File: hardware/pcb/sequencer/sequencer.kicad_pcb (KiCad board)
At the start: 2 copper layers, 106 parts, among them J1 Conn_02x08_Counter_Clockwise, J2 Conn_02x08_Counter_Clockwise, SW1 SW_SPST, SW10 SW_SPST, SW11 SW_SPST, SW12 SW_SPST, SW13 SW_SPST, SW14 SW_SPST, SW15 SW_SPST, SW16 SW_SPST, SW17 SW_SPST, SW18 SW_SPST, SW19 SW_SPST, SW2 SW_SPST, SW20 SW_SPST, SW21 SW_SPST, SW22 SW_SPST, SW23 SW_SPST, SW24 SW_SPST, SW3 SW_SPST, SW4 SW_SPST, SW5 SW_SPST, SW6 SW_SPST, SW7 SW_SPST, SW8 SW_SPST, SW9 SW_SPST

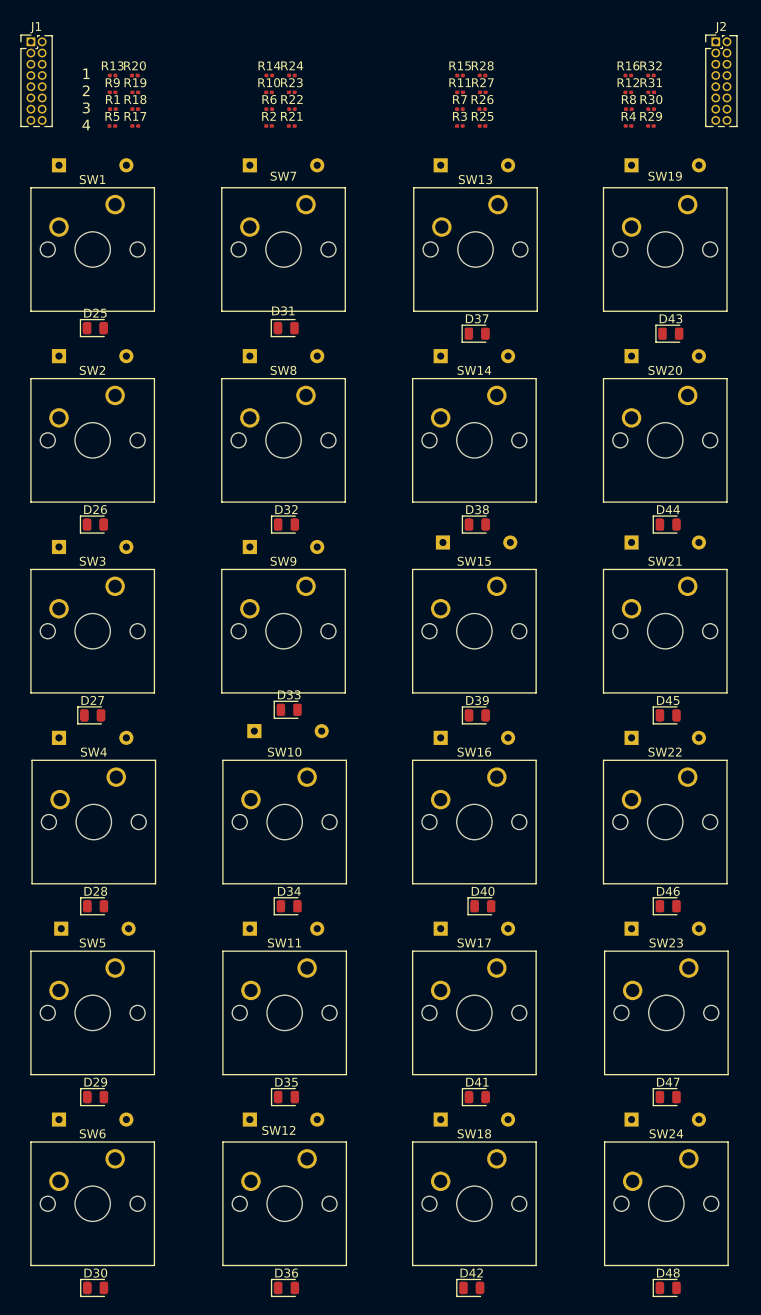
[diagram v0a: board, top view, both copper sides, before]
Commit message: sequencer: update pcb layout
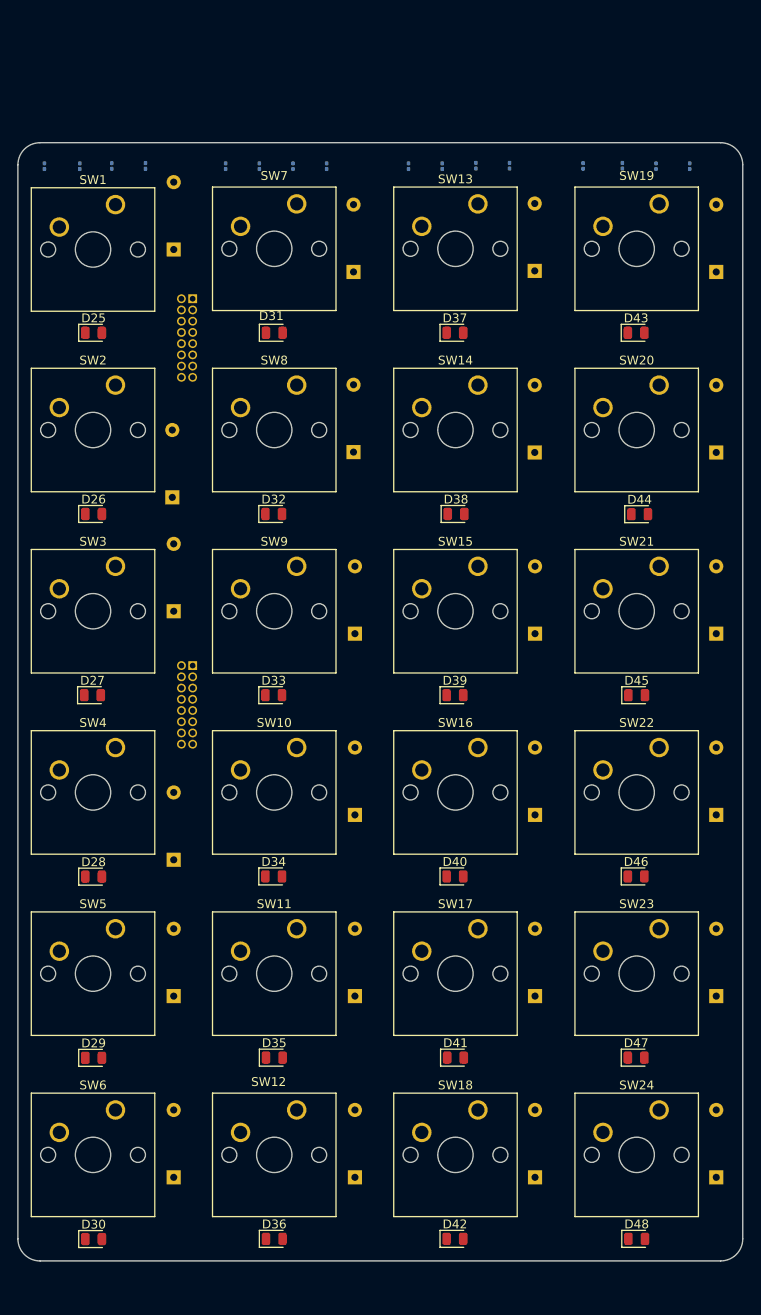
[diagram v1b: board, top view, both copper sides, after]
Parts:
- removed R17, R18, R19, R20, R21, R22, R23, R24, R25, R26, R27, R28, R29, R30, R31, R32: R, Resistor_SMD:R_0201_0603Metric
- J1, J2: value Conn_02x08_Counter_Clockwise -> Conn_02x08_Odd_Even; moved to B.Cu
- S1: renamed from R13; moved to B.Cu
- S10: renamed from R6; moved to B.Cu
- S11: renamed from R7; moved to B.Cu
- S12: renamed from R8; moved to B.Cu
- S13: renamed from R1; moved to B.Cu
- S14: renamed from R2; moved to B.Cu
- S15: renamed from R3; moved to B.Cu
- S16: renamed from R4; moved to B.Cu
- S2: renamed from R14; moved to B.Cu
- S3: renamed from R15; moved to B.Cu
- S4: renamed from R16; moved to B.Cu
- S5: renamed from R9; moved to B.Cu
- S6: renamed from R10; moved to B.Cu
- S7: renamed from R11; moved to B.Cu
- S8: renamed from R12; moved to B.Cu
- S9: renamed from R5; moved to B.Cu
- moved J2 92.1 mm to (72.3, 115.7), turned to 180 degrees
- moved J1 34.3 mm to (72.3, 74.2), turned to 180 degrees
- moved D2 20.5 mm to (70.0, 96.6), turned to 90 degrees
- moved D4 18.9 mm to (70.1, 137.6), turned to 90 degrees
- moved D7 16.8 mm to (90.5, 71.1), turned to 90 degrees
- moved D1 16.1 mm to (70.1, 68.6), turned to 90 degrees
- moved D13 16.0 mm to (111.0, 71.0), turned to 90 degrees
- moved D8 16.0 mm to (90.5, 91.5), turned to 90 degrees
- moved D9 15.4 mm to (90.6, 112.0), turned to 90 degrees
- moved D19 15.4 mm to (131.5, 71.1), turned to 90 degrees
- moved D14 15.2 mm to (111.0, 91.5), turned to 90 degrees
- moved D3 14.9 mm to (70.1, 109.5), turned to 90 degrees
- moved D5 14.8 mm to (70.1, 153.0), turned to 90 degrees
- moved D10 14.8 mm to (90.6, 132.5), turned to 90 degrees
- moved D15 14.7 mm to (111.0, 112.0), turned to 90 degrees
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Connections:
- D25 pad 2: Net-(D25-A) -> C1
- D26 pad 2: Net-(D25-A) -> C1
- D27 pad 2: Net-(D25-A) -> C1
- D28 pad 2: Net-(D25-A) -> C1
- D29 pad 2: Net-(D25-A) -> C1
- D30 pad 2: Net-(D25-A) -> C1
- D31 pad 2: Net-(D31-A) -> C2
- D32 pad 2: Net-(D31-A) -> C2
- D33 pad 2: Net-(D31-A) -> C2
- D34 pad 2: Net-(D31-A) -> C2
- D35 pad 2: Net-(D31-A) -> C2
- D36 pad 2: Net-(D31-A) -> C2
- D37 pad 2: Net-(D37-A) -> C3
- D38 pad 2: unconnected-(D38-A-Pad2) -> C3
- D39 pad 2: unconnected-(D39-A-Pad2) -> C3
- D40 pad 2: unconnected-(D40-A-Pad2) -> C3
- D41 pad 2: unconnected-(D41-A-Pad2) -> C3
- D42 pad 2: Net-(D37-A) -> C3
- D43 pad 2: Net-(D43-A) -> C4
- D44 pad 2: Net-(D43-A) -> C4
- D45 pad 2: Net-(D43-A) -> C4
- D46 pad 2: Net-(D43-A) -> C4
- D47 pad 2: Net-(D43-A) -> C4
- D48 pad 2: Net-(D43-A) -> C4
- J1 pad 10: I10 -> I13
- J1 pad 11: I11 -> I6
- J1 pad 12: I12 -> I14
- J1 pad 13: I13 -> I7
- J1 pad 14: I14 -> I15
- J1 pad 15: I15 -> I8
- J1 pad 2: I2 -> I9
- J1 pad 3: I3 -> I2
- J1 pad 4: I4 -> I10
- J1 pad 5: I5 -> I3
- J1 pad 6: I6 -> I11
- J1 pad 7: I7 -> I4
- J1 pad 8: I8 -> I12
- J1 pad 9: I9 -> I5
- J2 pad 10: O10 -> O13
- J2 pad 11: O11 -> O6
- J2 pad 12: O12 -> O14
- J2 pad 13: O13 -> O7
- J2 pad 14: O14 -> O15
- J2 pad 15: O15 -> O8
- J2 pad 2: O2 -> O9
- J2 pad 3: O3 -> O2
- J2 pad 4: O4 -> O10
- J2 pad 5: O5 -> O3
- J2 pad 6: O6 -> O11
- J2 pad 7: O7 -> O4
- J2 pad 8: O8 -> O12
- J2 pad 9: O9 -> O5
- S1 pad 2: Net-(SW1-B) -> C1
- S10 pad 2: Net-(SW10-B) -> C2
- S11 pad 2: Net-(SW13-B) -> C3
- S12 pad 2: Net-(SW19-B) -> C4
- S13 pad 2: Net-(SW1-B) -> C1
- S14 pad 2: Net-(SW10-B) -> C2
- S15 pad 2: Net-(SW13-B) -> C3
- S16 pad 2: Net-(SW19-B) -> C4
- S2 pad 2: Net-(SW10-B) -> C2
- S3 pad 2: Net-(SW13-B) -> C3
- S4 pad 2: Net-(SW19-B) -> C4
- S5 pad 2: Net-(SW1-B) -> C1
- S6 pad 2: Net-(SW10-B) -> C2
- S7 pad 2: Net-(SW13-B) -> C3
- S8 pad 2: Net-(SW19-B) -> C4
- S9 pad 2: Net-(SW1-B) -> C1
- SW1 pad 2: Net-(SW1-B) -> C1
- SW10 pad 2: Net-(SW10-B) -> C2
- SW11 pad 2: Net-(SW10-B) -> C2
- SW12 pad 2: Net-(SW10-B) -> C2
- SW13 pad 2: Net-(SW13-B) -> C3
- SW14 pad 2: Net-(SW13-B) -> C3
- SW15 pad 2: Net-(SW13-B) -> C3
- SW16 pad 2: Net-(SW13-B) -> C3
- SW17 pad 2: Net-(SW13-B) -> C3
- SW18 pad 2: Net-(SW13-B) -> C3
- SW19 pad 2: Net-(SW19-B) -> C4
- SW2 pad 2: Net-(SW1-B) -> C1
- SW20 pad 2: Net-(SW19-B) -> C4
- SW21 pad 2: Net-(SW19-B) -> C4
- SW22 pad 2: Net-(SW19-B) -> C4
- SW23 pad 2: Net-(SW19-B) -> C4
- SW24 pad 2: Net-(SW19-B) -> C4
- SW3 pad 2: Net-(SW1-B) -> C1
- SW4 pad 2: Net-(SW1-B) -> C1
- SW5 pad 2: Net-(SW1-B) -> C1
- SW6 pad 2: Net-(SW1-B) -> C1
- SW7 pad 2: Net-(SW10-B) -> C2
- SW8 pad 2: Net-(SW10-B) -> C2
- SW9 pad 2: Net-(SW10-B) -> C2
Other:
- board outline added: 82 x 126.5 mm
- board text added: "INPUT"
- board text added: "OUTPUT"
- board text removed: "1 2 3 4"

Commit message: sequencer: route pcb
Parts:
- S1, S10, S11, S12, S13, S14, S15, S16, S2, S3, S4, S5, S6, S7, S8, S9: footprint Resistor_SMD:R_0201_0603Metric -> Resistor_SMD:R_0603_1608Metric
- moved S16 54.9 mm to (61.5, 58.8)
- moved S1 53.1 mm to (120.0, 58.8)
- moved S12 43.4 mm to (77.5, 58.8)
- moved S5 41.9 mm to (105.0, 58.8)
- moved S15 31.2 mm to (65.5, 58.8)
- moved S8 31.2 mm to (93.5, 58.8)
- moved S9 30.0 mm to (89.5, 58.8)
- moved S2 29.1 mm to (116.5, 58.8)
- moved J1 23.2 mm to (92.3, 62.5)
- moved J2 20.2 mm to (92.5, 115.7)
- moved S4 19.5 mm to (109.0, 58.8)
- moved S11 19.0 mm to (81.5, 58.8)
- moved S13 18.0 mm to (73.5, 58.8)
- moved S6 17.4 mm to (101.0, 58.8)
- moved D7 13.4 mm to (90.5, 84.5)
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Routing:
- net C2: track 0.00 -> 220.6 mm, vias 0 -> 12
- net C1: track 0.00 -> 210.9 mm, vias 0 -> 6
- net C3: track 0.00 -> 207.9 mm, vias 0 -> 14
- net C4: track 0.00 -> 206.9 mm, vias 0 -> 5
- net O14: track 0.00 -> 121.8 mm, vias 0 -> 1
- net O6: track 0.00 -> 114.4 mm
- net O9: track 0.00 -> 106.9 mm, vias 0 -> 1
- net O13: track 0.00 -> 104.0 mm, vias 0 -> 1
- net O1: track 0.00 -> 103.7 mm, vias 0 -> 2
- net O5: track 0.00 -> 97.5 mm, vias 0 -> 1
- net O12: track 0.00 -> 86.9 mm, vias 0 -> 1
- net O2: track 0.00 -> 86.3 mm, vias 0 -> 1
- net O4: track 0.00 -> 85.3 mm, vias 0 -> 1
- net O10: track 0.00 -> 83.4 mm, vias 0 -> 1
- net O3: track 0.00 -> 73.7 mm, vias 0 -> 1
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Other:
- board size 82 x 126.5 mm -> 82 x 130.2 mm
- board text added: "S15"
- board text added: "SOLDER BRIDGES 1: S1 S5 S9 S13 2: S2 S6 S10 S14 3: S3 S7 S11 S15 4: S4 S8 S12 S16"

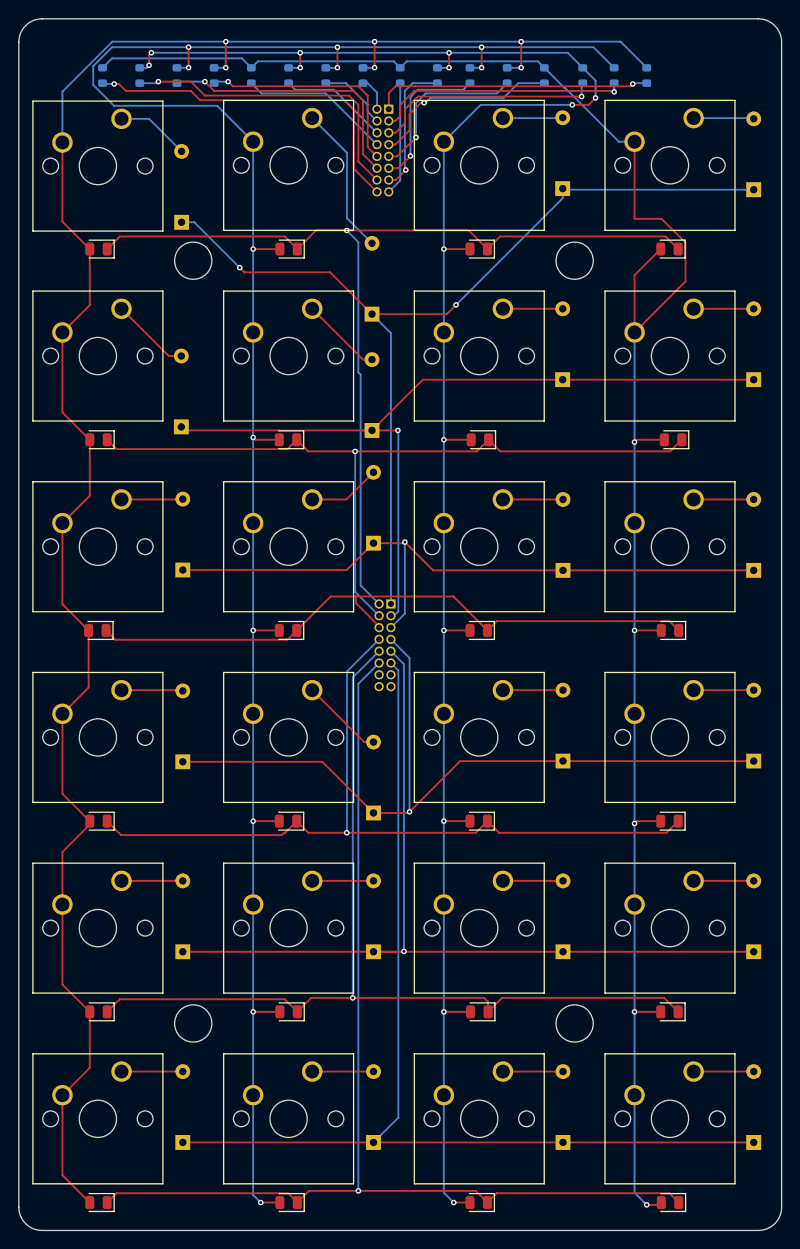
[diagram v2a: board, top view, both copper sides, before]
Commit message: sequencer: redue board size
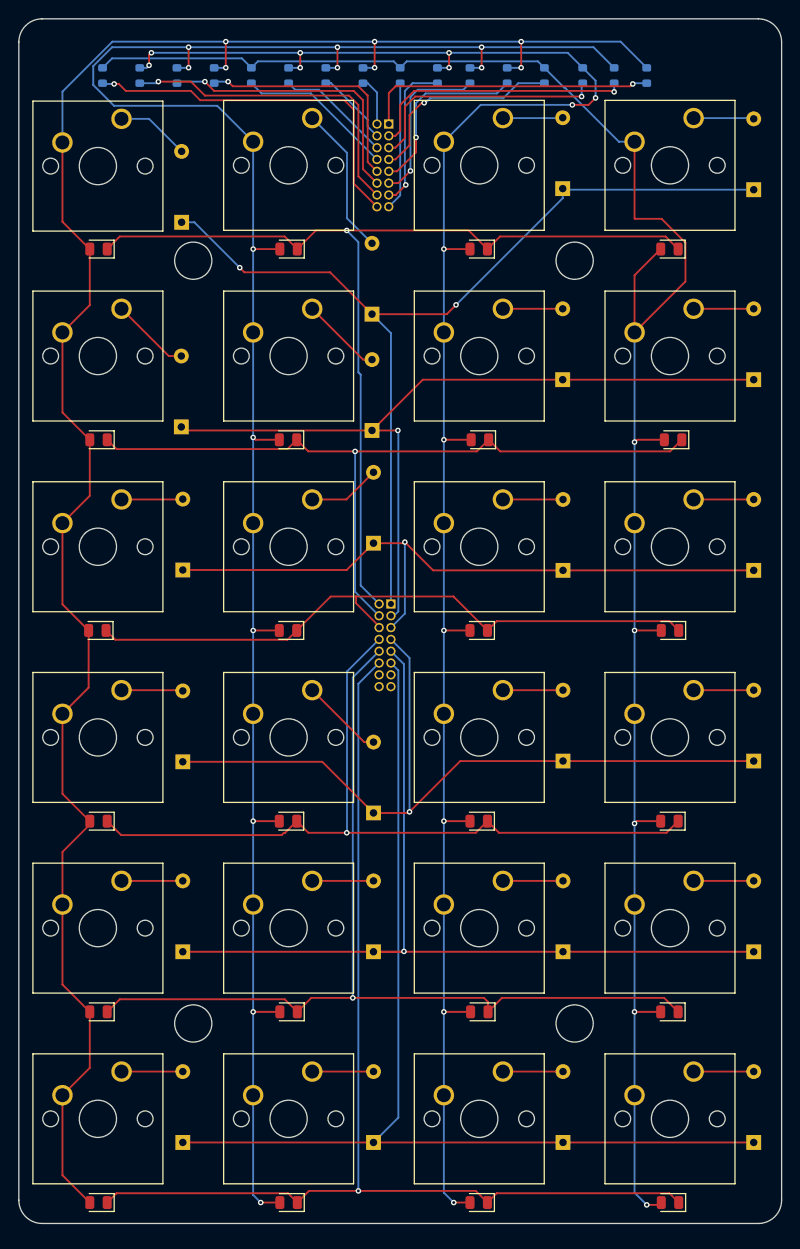
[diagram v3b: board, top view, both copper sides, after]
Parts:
- moved J1 1.60 mm to (92.3, 64.1)
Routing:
- net I3: track 24.7 -> 26.5 mm
- net I16: track 38.1 -> 39.7 mm
- net I15: track 33.5 -> 35.1 mm
- net I8: track 12.2 -> 13.8 mm
- net I9: track 3.71 -> 5.31 mm
- net I7: track 14.7 -> 16.3 mm
- net I2: track 27.2 -> 28.8 mm
- net I1: track 29.9 -> 31.5 mm
- net I6: track 16.2 -> 17.8 mm
- net I5: track 18.2 -> 19.8 mm
- net I14: track 28.6 -> 30.2 mm
- net I13: track 23.7 -> 25.3 mm
- net I4: track 20.5 -> 22.0 mm
- net I12: track 16.2 -> 16.9 mm
- net I10: track 7.61 -> 8.27 mm
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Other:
- board size 82 x 130.2 mm -> 82 x 129.5 mm
- board text added: "ADDRESS"
- board text added: "DATA"
- board text removed: "INPUT"
- board text removed: "OUTPUT"

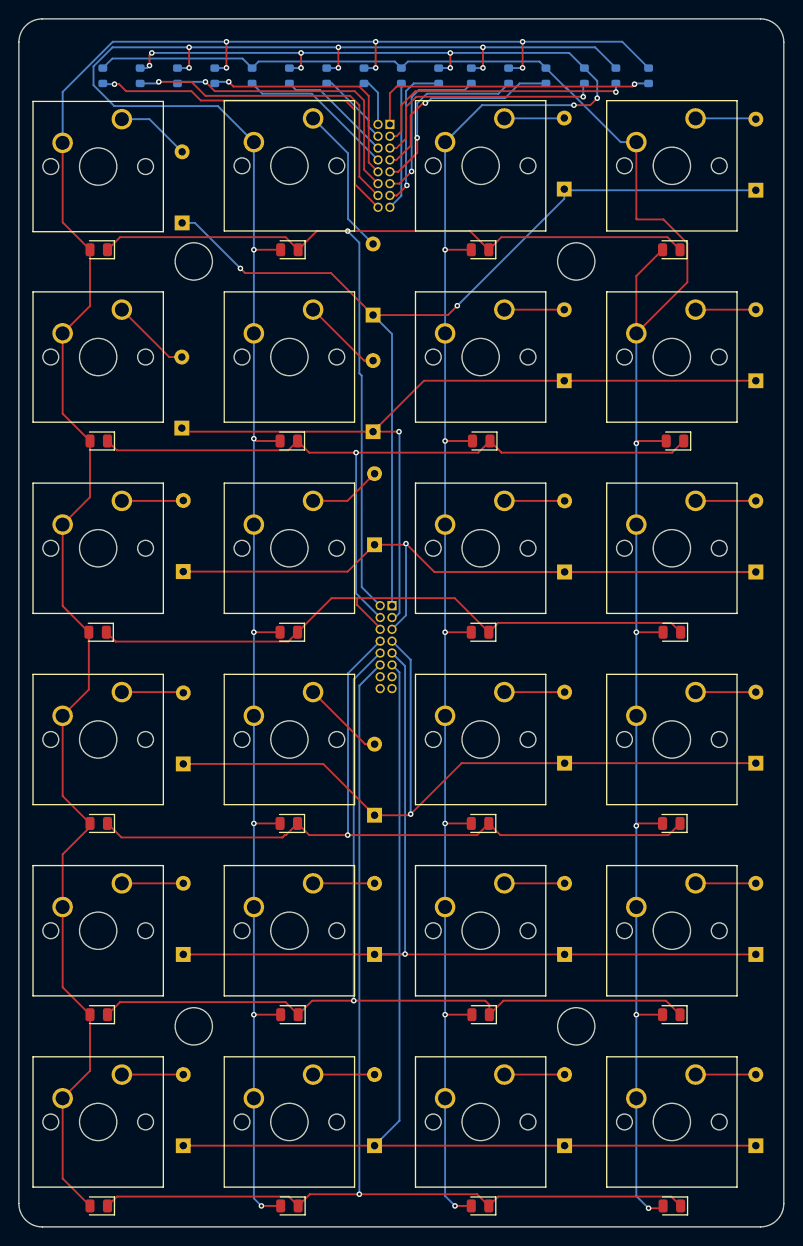
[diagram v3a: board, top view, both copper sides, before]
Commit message: hardware: add schematics
add controls, io, keys, and nucleo hat boards
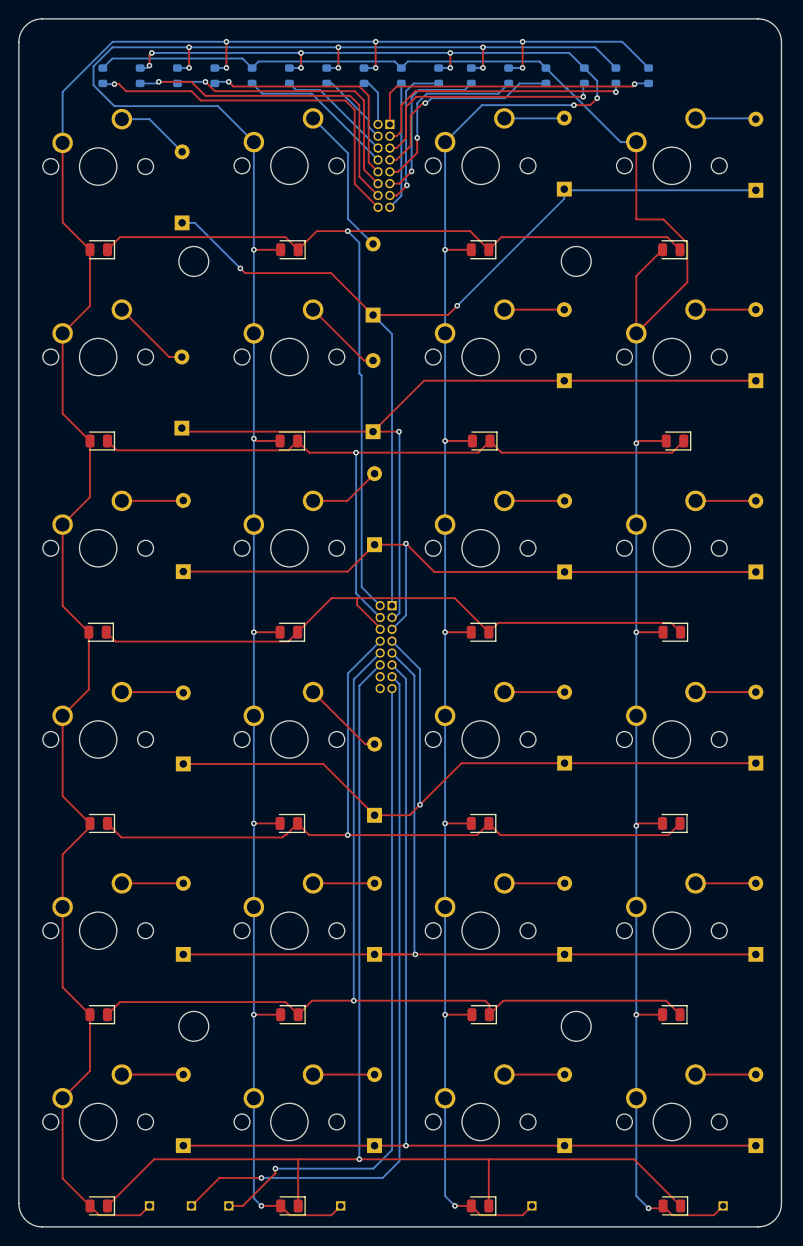
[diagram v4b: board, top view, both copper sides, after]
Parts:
- added COL: Conn_01x01, Connector_PinHeader_1.27mm:PinHeader_1x01_P1.27mm_Vertical, B.Cu at (87.0, 180.0)
- added COL: Conn_01x01, Connector_PinHeader_1.27mm:PinHeader_1x01_P1.27mm_Vertical, B.Cu at (107.5, 180.0)
- added COL: Conn_01x01, Connector_PinHeader_1.27mm:PinHeader_1x01_P1.27mm_Vertical, B.Cu at (66.5, 180.0)
- added COL: Conn_01x01, Connector_PinHeader_1.27mm:PinHeader_1x01_P1.27mm_Vertical, B.Cu at (128.0, 180.0)
- added ROW7: Conn_01x01, Connector_PinHeader_1.27mm:PinHeader_1x01_P1.27mm_Vertical, B.Cu at (71.0, 180.0)
- added ROW8: Conn_01x01, Connector_PinHeader_1.27mm:PinHeader_1x01_P1.27mm_Vertical, B.Cu at (75.0, 180.0)
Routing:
- net O7: track 0.00 -> 76.6 mm, vias 0 -> 1
- net O8: track 0.00 -> 69.7 mm, vias 0 -> 1
- net O14: track 121.8 -> 129.6 mm
- net C3: track 207.9 -> 215.2 mm
- net C2: track 220.6 -> 227.9 mm
- net C4: track 206.9 -> 214.1 mm
- net C1: track 210.9 -> 218.2 mm
- net O6: track 114.4 -> 113.5 mm, vias 0 -> 1
- net O4: track 85.3 -> 84.7 mm
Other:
- board size 82 x 129.5 mm -> 81.8 x 129.5 mm
